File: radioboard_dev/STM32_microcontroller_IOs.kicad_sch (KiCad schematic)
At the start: 31 parts

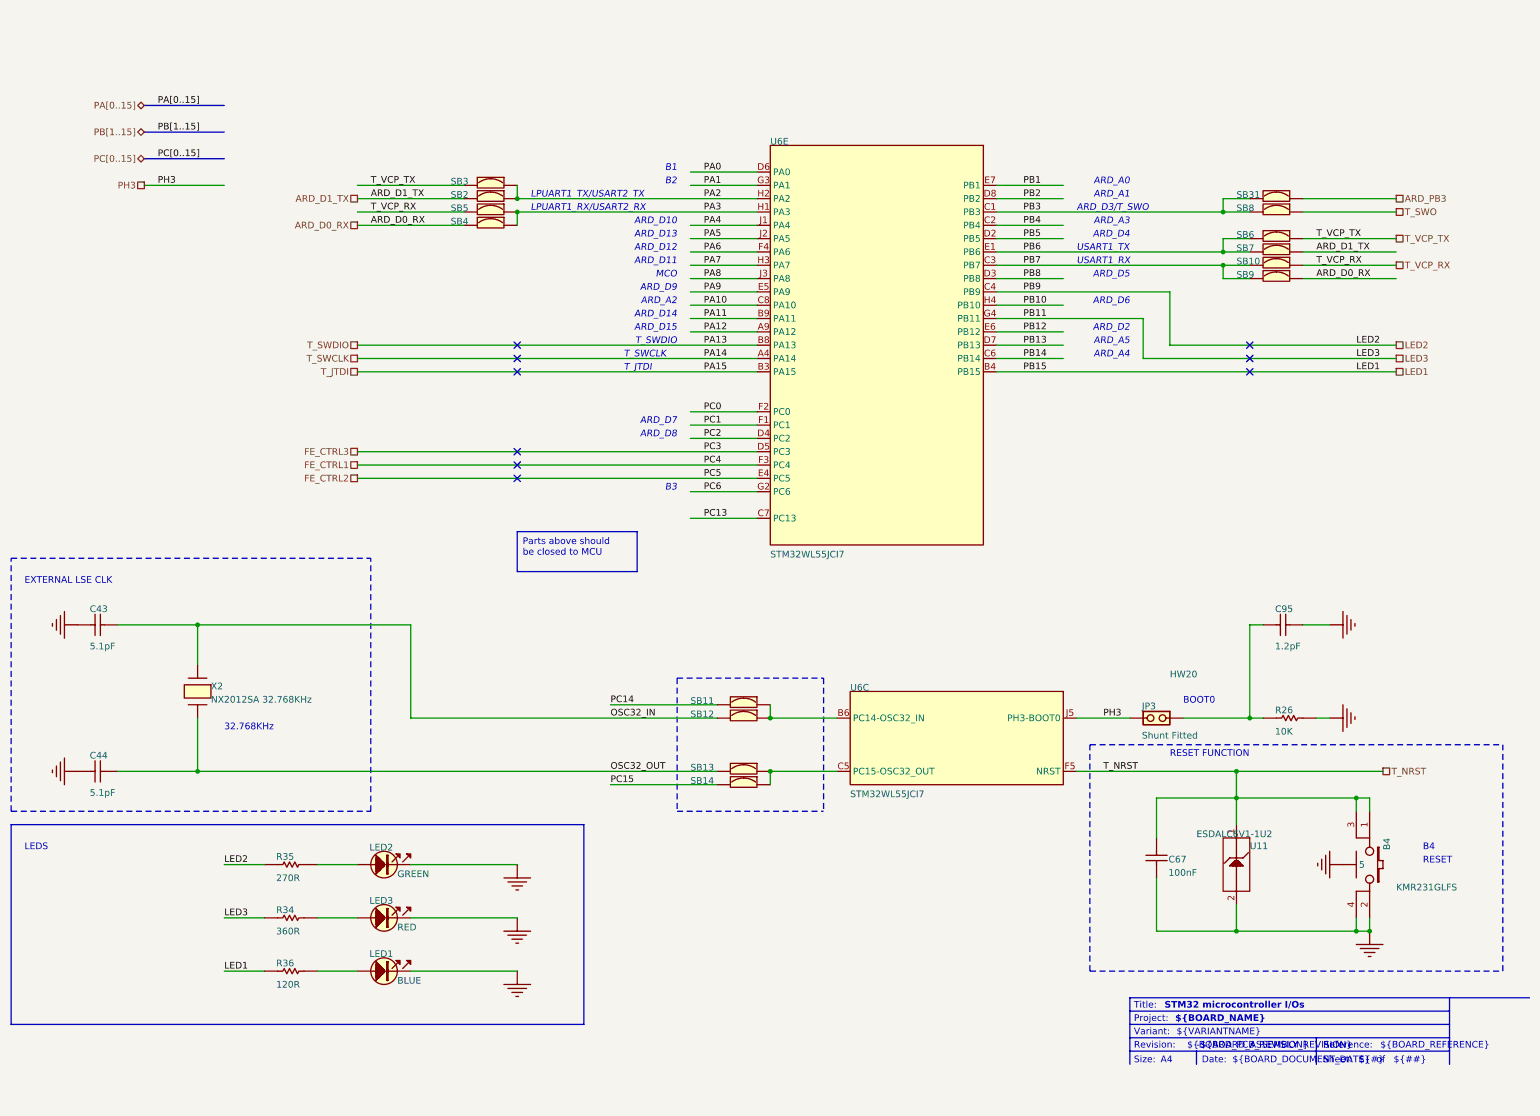
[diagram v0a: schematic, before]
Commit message: added components
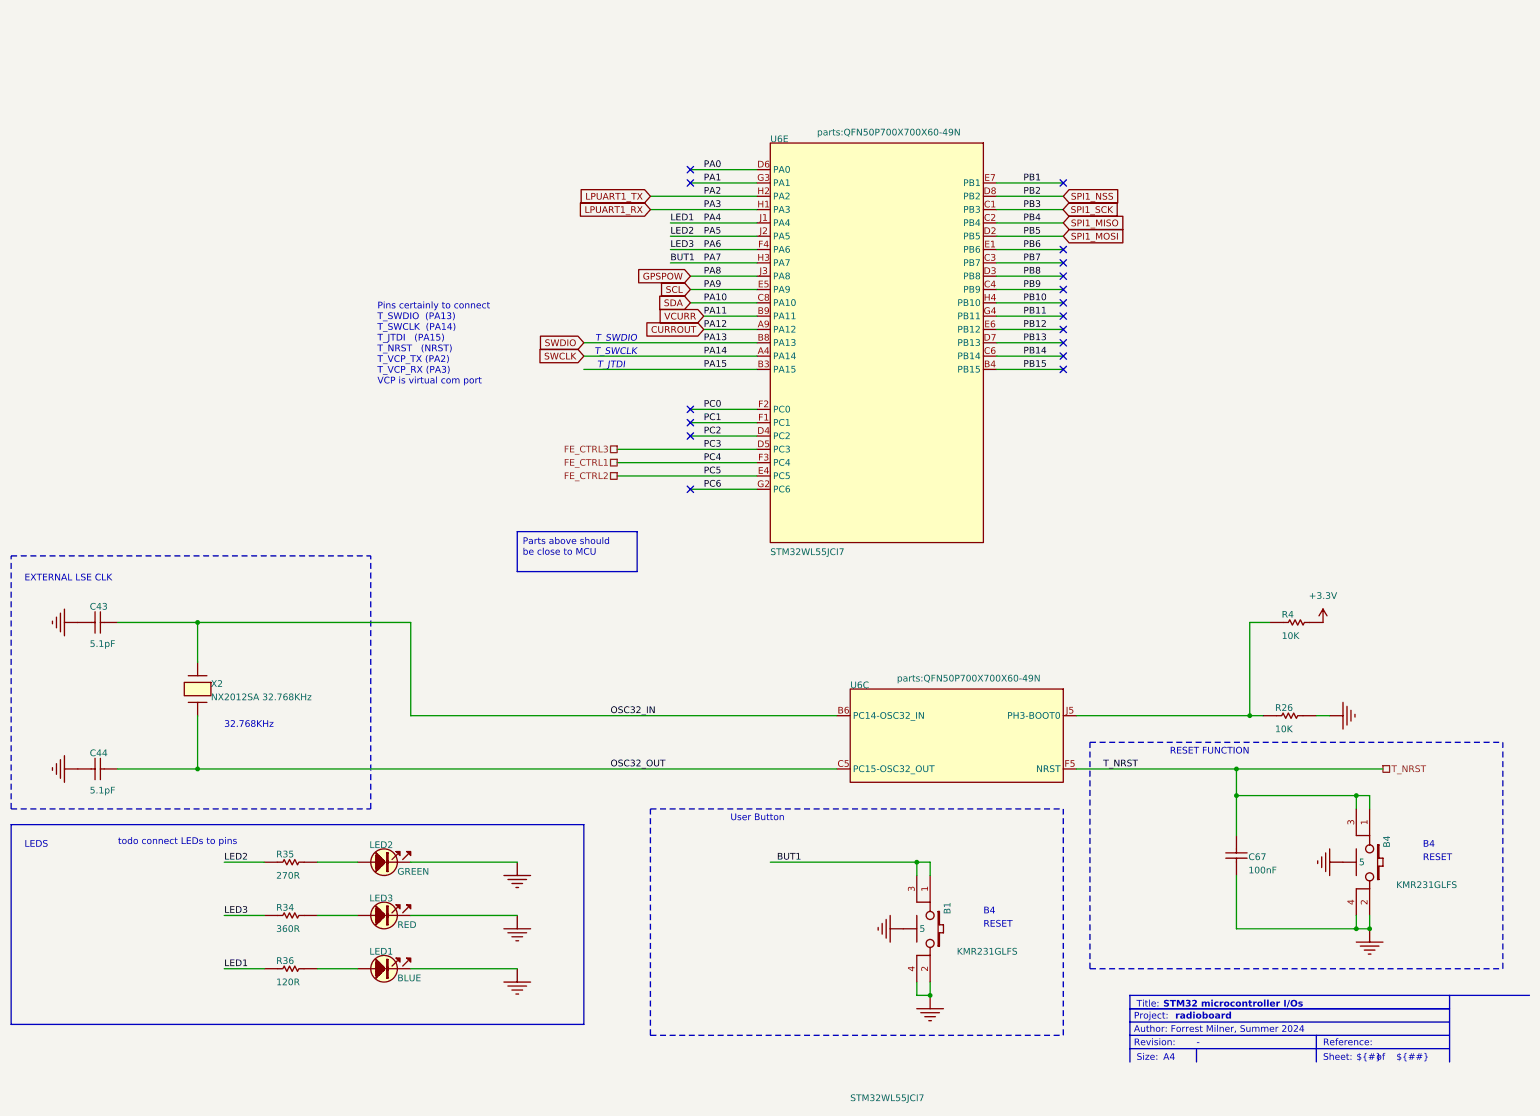
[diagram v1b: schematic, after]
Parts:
- removed C95: Capacitor, C0402, symbol MB1389-altium-import:U_STM32_microcontroller_IOs_2_Capacitor
- removed JP3: (no value), CON_SAMTEC_TSW-102-07-G-S, symbol MB1389-altium-import:U_STM32_microcontroller_IOs_0_Jumper_Header 2x1 Fitted
- removed SB10, SB11, SB12, SB13, SB14, SB3, SB31, SB5, SB6, SB8: (no value), SOLDER-BRIDGE_R0603-0R, symbol MB1389-altium-import:U_STM32_microcontroller_IOs_0_SB_ON
- removed SB2, SB4, SB7, SB9: (no value), SOLDER-BRIDGE_R0603-0R, symbol MB1389-altium-import:U_STM32_microcontroller_IOs_0_mirrored_SB_ON
- removed U11: (no value), ESD_ST0201, symbol MB1389-altium-import:U_STM32_microcontroller_IOs_0_ESD-TRANSIL
- added B1: ~, parts:SWI_C&K_Y78B23110FP__ITT_KMR231GLFS, symbol MB1389-altium-import:U_STM32_microcontroller_IOs_3_SW-PUSH-CMS_KMR2_BLACK
- added R4: ~, parts:R0603, symbol MB1389-altium-import:U_STM32_microcontroller_IOs_2_Resistor
- B4: value (none) -> ~; footprint SWI_C&K_Y78B23110FP__ITT_KMR231GLFS -> parts:SWI_C&K_Y78B23110FP__ITT_KMR231GLFS
- C43, C44, HW20, LED1, LED2, LED3, R34, R35, R36: value (none) -> ~
- C67: value (none) -> ~; footprint C0402 -> parts:C0402
- R26: value (none) -> ~; footprint R0603 -> parts:R0603
- U6: value (none) -> ~; footprint ICC_UFBGA73_5X5_P050 -> parts:QFN50P700X700X60-49N
- X2: value (none) -> ~; footprint CRY_NX2012SA_2P -> parts:CRY_NX2012SA_2P
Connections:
- net PA4 is gone; now on net LED1: U6.J1 (PA4)
- net PA5 is gone; now on net LED2: U6.J2 (PA5)
- net PA6 is gone; now on net LED3: U6.F4 (PA6)
- net PH3 is gone; now on an unnamed net: U6.J5 (PH3-BOOT0)
- net GND: now also B1.2, B1.4, B1.5
- net LED1: no longer U6.B4 (PB15)
- net LED2: no longer U6.C4 (PB9)
- net LED3: no longer U6.G4 (PB11)
- net OSC32_IN: now also U6.B6 (PC14-OSC32_IN)
- net OSC32_OUT: now also U6.C5 (PC15-OSC32_OUT)
- net at R26.2: now also R4.2
- net PA10 renamed SDA
- net PA11 renamed VCURR
- net PA12 renamed CURROUT
- net PA2 renamed LPUART1_TX
- net PA3 renamed LPUART1_RX
- net PA7 renamed BUT1
- net BUT1: now also B1.1, B1.3
- net PA8 renamed GPSPOW
- net PA9 renamed SCL
- net PB2 renamed SPI1_NSS
- net PB3 renamed SPI1_SCK
- net PB4 renamed SPI1_MISO
- net PB5 renamed SPI1_MOSI
- removed net PC13: U6.C7 (PC13)
- net T_JTDI renamed PA15
- net T_SWCLK renamed SWCLK
- net T_SWDIO renamed SWDIO
- new net +3.3V: R4.1
- new net PB11: U6.G4 (PB11)
- new net PB15: U6.B4 (PB15)
- new net PB9: U6.C4 (PB9)
- no-connect marks 9 -> 17
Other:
- note added: "Author: Forrest Milner, Summer 2024"
- note added: "Pins certainly to connect T_SWDIO (PA13) T_SWCLK (PA14) T_JTDI (PA15) T_NRST (NRST) T_VCP_TX (PA2) T_VCP_RX (PA3) VCP is virtual com port"
- note added: "User Button"
- note added: "radioboard"
- note added: "todo connect LEDs to pins"
- note removed: "${BOARD_ASSEMBLY_REVISION}"
- note removed: "${BOARD_DOCUMENT_DATE}"
- note removed: "${BOARD_NAME}"
- note removed: "${BOARD_PCB_REVISION}"
- note removed: "${BOARD_REFERENCE}"
- note removed: "${VARIANTNAME}"
- note removed: "ARD_A0"
- note removed: "ARD_A1"
- note removed: "ARD_A2"
- note removed: "ARD_A3"
- note removed: "ARD_A4"
- note removed: "ARD_A5"
- note removed: "ARD_D10"
- note removed: "ARD_D11"
- note removed: "ARD_D12"
- note removed: "ARD_D13"
- note removed: "ARD_D14"
- note removed: "ARD_D15"
- note removed: "ARD_D2"
- note removed: "ARD_D3/T_SWO"
- note removed: "ARD_D4"
- note removed: "ARD_D5"
- note removed: "ARD_D6"
- note removed: "ARD_D7"
- note removed: "ARD_D8"
- note removed: "ARD_D9"
- note removed: "B1"
- note removed: "B2"
- note removed: "B3"
- note removed: "BOOT0"
- note removed: "Date:"
- note removed: "LPUART1_RX/USART2_RX"
- note removed: "LPUART1_TX/USART2_TX"
- note removed: "MCO"
- note removed: "USART1_RX"
- note removed: "USART1_TX"
- note removed: "Variant:"
- moved on the sheet: C67

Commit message: finish schematic and clear pcb
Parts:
- removed U6: ~, parts:QFN50P700X700X60-49N, symbol MB1389-altium-import:U_STM32_microcontroller_IOs_0_STM32WL5x_BGA73
- added C10, C18, C23, C28: ~, parts:C0402, symbol MB1389-altium-import:U_STM32_microcontroller_power_1_Capacitor
- added C26: ~, parts:C0603, symbol MB1389-altium-import:U_STM32_microcontroller_power_1_Capacitor
- added L1: ~, parts:L0603, symbol MB1389-altium-import:U_STM32_microcontroller_power_0_BEAD
- added U10: STM32WL55CCUx, Package_DFN_QFN:QFN-48-1EP_7x7mm_P0.5mm_EP5.6x5.6mm, symbol MCU_ST_STM32WL:STM32WL55CCUx
- R4: now not fitted; now left out of the parts list
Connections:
- net +3.3V: now also L1.1
- net BUT1: now also U10.15 (PA7)
- net CURROUT: now also U10.35 (PA12)
- net FE_CTRL1: now also U10.4 (PB6)
- net FE_CTRL2: now also U10.5 (PB7)
- net FE_CTRL3: now also U10.6 (PB8)
- net GND: now also C10.2, C18.2, C23.2, C26.1, C28.1, U10.48 (VSSSMPS), U10.49 (VSS)
- net GPSPOW: now also U10.16 (PA8)
- net LED1: now also U10.12 (PA4)
- net LED2: now also U10.13 (PA5)
- net LED3: now also U10.14 (PA6)
- net LPUART1_RX: now also U10.10 (PA3)
- net LPUART1_TX: now also U10.9 (PA2)
- net OSC32_IN: now also U10.39 (PC14)
- net OSC32_OUT: now also U10.40 (PC15)
- net SCL: now also U10.17 (PA9)
- net SDA: now also U10.33 (PA10)
- net SPI1_MISO: now also U10.2 (PB4)
- net SPI1_MOSI: now also U10.3 (PB5)
- net SPI1_NSS: now also U10.31 (PB2)
- net SPI1_SCK: now also U10.1 (PB3)
- net SWCLK: now also U10.42 (PA14)
- net SWDIO: now also U10.36 (PA13)
- net VCURR: now also U10.34 (PA11)
- net BOOT0: now reaches R26.2, R4.2
- net BOOT0: now also U10.19 (PH3)
- net T_NRST renamed NRST
- net NRST: now also U10.18 (NRST)
- new net: C26.2, C28.2, L1.2, U10.41 (VDDA)
- new net: C10.1, C18.1, C23.1, U10.11 (VDD), U10.37 (VBAT), U10.44 (VDD)
- new net OSC_IN: U10.26 (OSC_IN)
- new net OSC_OUT: U10.27 (OSC_OUT)
- new net PB0_VDD_TCXO: U10.30 (PB0)
- new net RFI_N: U10.21 (RFI_N)
- new net RFI_P: U10.20 (RFI_P)
- new net RFO_HP: U10.23 (RFO_HP)
- new net RFO_LP: U10.22 (RFO_LP)
- new net VDDPA: U10.25 (VDDPA)
- new net VDDRF: U10.28 (VDDRF)
- new net VDDRF1V55: U10.29 (VDDRF1V55)
- new net VDDSMPS: U10.46 (VDDSMPS)
- new net VFBSMPS: U10.45 (VFBSMPS)
- new net VLXSMPS: U10.47 (VLXSMPS)
- new net VR_PA: U10.24 (VR_PA)
- no-connect marks 17 -> 5
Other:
- note removed: "T_JTDI"
- note removed: "T_SWCLK"
- note removed: "T_SWDIO"

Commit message: footprints
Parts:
- removed LED1: ~, LED_0603_OSRAM_LB-Q39G-L2OO-35-1_BLUE_1A2K_H0P4, symbol MB1389-altium-import:U_STM32_microcontroller_IOs_0_LED_blue_0
- removed R36: ~, R0402, symbol MB1389-altium-import:U_STM32_microcontroller_IOs_0_Resistor
- LED3: footprint LED_0603_VISHAY_VLMS1300-GS08_RED_1A2K_H0P8 -> parts:LED_0603_VISHAY_VLMS1300-GS08_RED_1A2K_H0P8
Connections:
- net +3.3V: now also C10.1, C18.1, C23.1, U10.11 (VDD), U10.37 (VBAT), U10.44 (VDD)
- net LED1: now also R35.1
- net LED2: now also R34.1; no longer R35.1
- net LED3: no longer names the net of U10.14 (PA6)
- net LED3: no longer R34.1
- no-connect marks 5 -> 6

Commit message: all footprints done
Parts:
- removed X2: ~, parts:CRY_NX2012SA_2P, symbol MB1389-altium-import:U_STM32_microcontroller_IOs_0_XTAL_2_PINS
- added XTAL2: NX2012SA-32.768K-STD-MUB-1, parts:XTAL_NX2012SA_NDK, symbol XTAL_NX2012SA_NDK:NX2012SA-32.768K-STD-MUB-1
- L1: footprint parts:L0603 -> Inductor_SMD:L_0603_1608Metric
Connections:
- net OSC32_IN: now also XTAL2.2
- net OSC32_OUT: now also XTAL2.1
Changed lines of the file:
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@@
 	(wire
 		(pts
-			(xy 38.1 133.35) (xy 38.1 125.73)
+			(xy 38.1 134.62) (xy 38.1 125.73)
 		)
 		(stroke
@@
 	(wire
 		(pts
-			(xy 38.1 153.67) (xy 38.1 143.51)
+			(xy 38.1 153.67) (xy 38.1 144.78)
 		)
 		(stroke
@@
 			)
 		)
-		(property "Footprint" "parts:L0603"
+		(property "Footprint" "Inductor_SMD:L_0603_1608Metric"
 			(at 198.12 20.32 0)
 			(effects
@@
 	)
 	(symbol
+		(lib_id "XTAL_NX2012SA_NDK:NX2012SA-32.768K-STD-MUB-1")
+		(at 38.1 144.78 90)
+		(unit 1)
+		(exclude_from_sim no)
+		(in_bom yes)
+		(on_board yes)
+		(dnp no)
+		(fields_autoplaced yes)
+		(property "Reference" "XTAL2"
+			(at 41.91 138.4299 90)
+			(effects
+				(font
+					(size 1.524 1.524)
+				)
+				(justify right)
+			)
+		)
+		(property "Value" "NX2012SA-32.768K-STD-MUB-1"
+			(at 41.91 140.9699 90)
+			(effects
+				(font
+					(size 1.524 1.524)
+				)
+				(justify right)
+			)
+		)
+		(property "Footprint" "parts:XTAL_NX2012SA_NDK"
+			(at 38.1 144.78 0)
+			(effects
+				(font
+					(size 1.27 1.27)
+					(italic yes)
+				)
+				(hide yes)
+			)
+		)
+		(property "Datasheet" "NX2012SA-32.768K-STD-MUB-1"
+			(at 38.1 144.78 0)
+			(effects
+				(font
+					(size 1.27 1.27)
+					(italic yes)
+				)
+				(hide yes)
+			)
+		)
+		(property "Description" ""
+			(at 38.1 144.78 0)
+			(effects
+				(font
+					(size 1.27 1.27)
+				)
+				(hide yes)
+			)
+		)
+		(pin "2"
+		)
+		(pin "1"
+		)
+		(instances
+			(project ""
+				(path "/d463a497-8f2e-444e-8cd9-7512b15bd4f7/991445d1-ac72-4dc7-8e85-5e852498bc5d"
+					(reference "XTAL2")
+					(unit 1)
+				)
+			)
+		)
+	)
+	(symbol
 		(lib_id "MB1389-altium-import:U_STM32_microcontroller_IOs_0_LED_red_0")
 		(at 68.58 181.61 0)
@@
 					(unit 1)
 				)
-			)
-		)
-	)
-	(symbol
-		(lib_id "MB1389-altium-import:U_STM32_microcontroller_IOs_0_XTAL_2_PINS")
-		(at 38.1 138.43 0)
-		(unit 1)
-		(exclude_from_sim no)
-		(in_bom yes)
-		(on_board yes)
-		(dnp no)
-		(property "Reference" "X2"
-			(at 40.64 138.176 0)
-			(effects
-				(font
-					(size 1.27 1.27)
-				)
-				(justify left bottom)
-			)
-		)
-		(property "Value" "~"
-			(at 40.64 143.51 0)
-			(effects
-				(font
-					(size 1.27 1.27)
-				)
-				(justify left bottom)
-				(hide yes)
-			)
-		)
-		(property "Footprint" "parts:CRY_NX2012SA_2P"
-			(at 38.1 138.43 0)
-			(effects
-				(font
-					(size 1.27 1.27)
-				)
-				(hide yes)
-			)
-		)
-		(property "Datasheet" "https://www.digikey.com/en/products/detail/ndk-america-inc/STDMUB1-32-768K/4914433"
-			(at 38.1 138.43 0)
-			(effects
-				(font
-					(size 1.27 1.27)
-				)
-				(hide yes)
-			)
-		)
-		(property "Description" "Crystal 32.768kHz, 6pF, -+20ppm, 80Kohm max, SMD"
-			(at 38.1 138.43 0)
-			(effects
-				(font
-					(size 1.27 1.27)
-				)
-				(hide yes)
-			)
-		)
-		(property "REVISION" ""
-			(at 35.56 132.842 0)
-			(effects
-				(font
-					(size 1.27 1.27)
-				)
-				(justify left bottom)
-				(hide yes)
-			)
-		)
-		(property "INTERNAL_PART_NUMBER" "MCD-01479"
-			(at 35.56 132.842 0)
-			(effects
-				(font
-					(size 1.27 1.27)
-				)
-				(justify left bottom)
-				(hide yes)
-			)
-		)
-		(property "ALTIUM_VALUE" "NX2012SA 32.768KHz"
-			(at 40.64 140.716 0)
-			(effects
-				(font
-					(size 1.27 1.27)
-				)
-				(justify left bottom)
-			)
-		)
-		(property "STATUS" "Checked"
-			(at 35.56 130.302 0)
-			(effects
-				(font
-					(size 1.27 1.27)
-				)
-				(justify left bottom)
-				(hide yes)
-			)
-		)
-		(property "PART_TYPE" "Crystal_Osc"
-			(at 35.56 130.302 0)
-			(effects
-				(font
-					(size 1.27 1.27)
-				)
-				(justify left bottom)
-				(hide yes)
-			)
-		)
-		(property "MANUFACTURER_PART_NUMBER" "NX2012SA 32.768KHz EXS00A-MU00527"
-			(at 35.56 130.302 0)
-			(effects
-				(font
-					(size 1.27 1.27)
-				)
-				(justify left bottom)
-				(hide yes)
-			)
-		)
-		(property "MANUFACTURER" "NDK"
-			(at 35.56 130.302 0)
-			(effects
-				(font
-					(size 1.27 1.27)
-				)
-				(justify left bottom)
-				(hide yes)
-			)
-		)
-		(property "PACKAGE" "NX2012SA"
-			(at 35.56 130.302 0)
-			(effects
-				(font
-					(size 1.27 1.27)
-				)
-				(justify left bottom)
-				(hide yes)
-			)
-		)
-		(property "COMPONENTLINK1DESCRIPTION" "Datasheet"
-			(at 35.56 130.302 0)
-			(effects
-				(font
-					(size 1.27 1.27)
-				)
-				(justify left bottom)
-				(hide yes)
-			)
-		)
-		(property "COMPONENTLINK1URL" "http://tunmcdsvn.tun.st.com/Component_Datasheet_Library/Trunk/Crystal_Osc/NDK_NX2012SA 32.768KHz EXS00A-MU00527"
-			(at 35.56 130.302 0)
-			(effects
-				(font
-					(size 1.27 1.27)
-				)
-				(justify left bottom)
-				(hide yes)
-			)
-		)
-		(property "PROVIDED_BY" "SUBCO"
-			(at 35.56 130.302 0)
-			(effects
-				(font
-					(size 1.27 1.27)
-				)
-				(justify left bottom)
-				(hide yes)
-			)
-		)
-		(property "ORDER_CODE_DIGIKEY" "644-1352"
-			(at 35.56 130.302 0)
-			(effects
-				(font
-					(size 1.27 1.27)
-				)
-				(justify left bottom)
-				(hide yes)
-			)
-		)
-		(property "ECCN_US" "EAR99"
-			(at 35.56 130.302 0)
-			(effects
-				(font
-					(size 1.27 1.27)
-				)
-				(justify left bottom)
-				(hide yes)
-			)
-		)
-		(property "ECCN_EU" "NEC"
-			(at 35.56 130.302 0)
-			(effects
-				(font
-					(size 1.27 1.27)
-				)
-				(justify left bottom)
-				(hide yes)
-			)
-		)
-		(property "BMS_PART_NUMBER" "9157049"
-			(at 35.56 130.302 0)
-			(effects
-				(font
-					(size 1.27 1.27)
-				)
-				(justify left bottom)
-				(hide yes)
-			)
-		)
-		(pin "2"
-		)
-		(pin "1"
-		)
-		(instances
-			(project ""
-				(path "/d463a497-8f2e-444e-8cd9-7512b15bd4f7/991445d1-ac72-4dc7-8e85-5e852498bc5d"
-					(reference "X2")
-					(unit 1)
-				)

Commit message: done for day
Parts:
- C18: footprint parts:C0402 -> Capacitor_SMD:C_0402_1005Metric
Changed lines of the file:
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@@
 			)
 		)
-		(property "Footprint" "parts:C0402"
+		(property "Footprint" "Capacitor_SMD:C_0402_1005Metric"
 			(at 130.81 19.05 0)
 			(effects

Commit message: almost done!!!
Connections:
- net BUT1: now also U10.14 (PA6); no longer U10.15 (PA7)
- net FE_CTRL1: now also U10.6 (PB8); no longer U10.4 (PB6)
- net FE_CTRL2: now also U10.7 (PA0); no longer U10.5 (PB7)
- net FE_CTRL3: now also U10.8 (PA1); no longer U10.6 (PB8)
- net GPSPOW: now also U10.43 (PA15); no longer U10.16 (PA8)
- net SCL: now also U10.4 (PB6); no longer U10.17 (PA9)
- net SDA: now also U10.5 (PB7); no longer U10.33 (PA10)

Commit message: basically done
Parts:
- renumbered LED2 to LED1, LED3 to LED2
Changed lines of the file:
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@@
 		(on_board yes)
 		(dnp no)
-		(property "Reference" "LED3"
+		(property "Reference" "LED2"
 			(at 70.866 179.07 0)
 			(effects
@@
 			(project ""
 				(path "/d463a497-8f2e-444e-8cd9-7512b15bd4f7/991445d1-ac72-4dc7-8e85-5e852498bc5d"
-					(reference "LED3")
+					(reference "LED2")
 					(unit 1)
 				)
@@
 		(on_board yes)
 		(dnp no)
-		(property "Reference" "LED2"
+		(property "Reference" "LED1"
 			(at 70.866 168.91 0)
 			(effects
@@
 			(project ""
 				(path "/d463a497-8f2e-444e-8cd9-7512b15bd4f7/991445d1-ac72-4dc7-8e85-5e852498bc5d"
-					(reference "LED2")
+					(reference "LED1")
 					(unit 1)
 				)
